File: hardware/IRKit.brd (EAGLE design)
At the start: 54 x 56 mm, 71 parts, among them CN1 USB-CONNECTORMICROB, IC1 ATMEGA32U4AU, IC2 TLV70233DBVT, IC3 LM386MM-1, IC4 GS1011MXXS, SW1 EVQPUJ02K, T1 2SD1781K, T2 BSS138

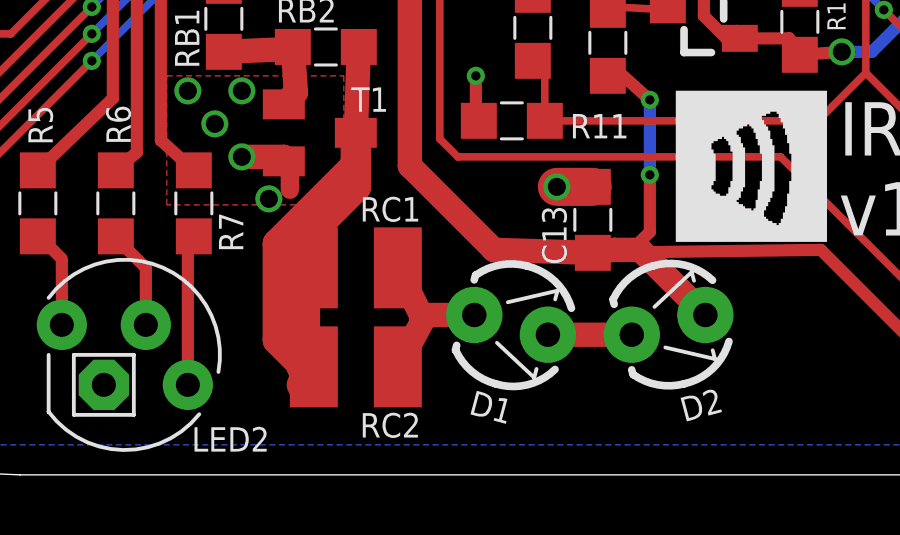
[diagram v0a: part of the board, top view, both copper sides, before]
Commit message: C13 1uF -> 4.7uF 1uF couldn't stop atmega32u4 from resetting when sending IR
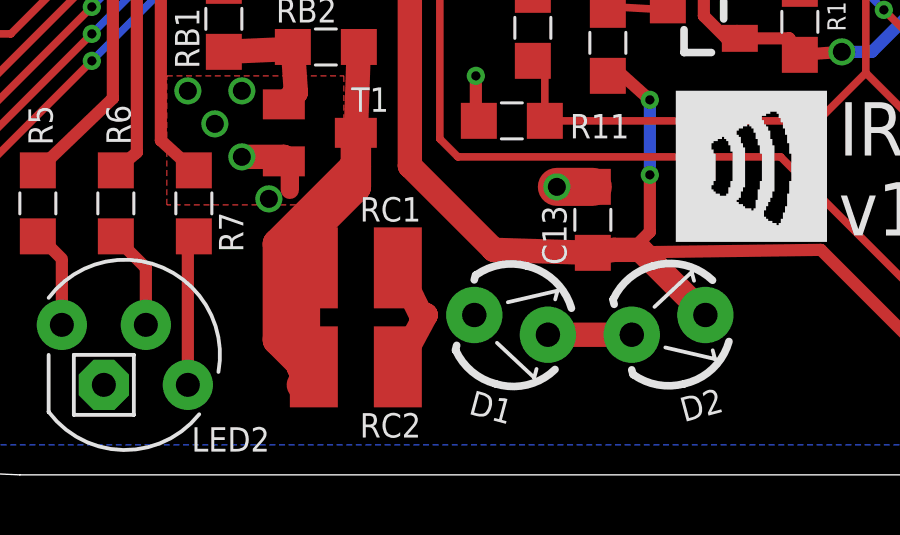
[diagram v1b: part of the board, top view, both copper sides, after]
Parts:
- C13: value 1uF -> 4.7uF
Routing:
- net IRLED: track 5.49 -> 3.87 mm
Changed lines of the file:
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@@
 <attribute name="VALUE" x="40.6" y="47.8" size="1.016" layer="27" rot="R180"/>
 </element>
-<element name="C13" library="my" package="SMD2012" value="1uF" x="27.1" y="8.5" smashed="yes" rot="R90">
+<element name="C13" library="my" package="SMD2012" value="4.7uF" x="27.1" y="8.5" smashed="yes" rot="R90">
 <attribute name="NAME" x="26.225" y="7" size="0.8128" layer="25" rot="R90"/>
 <attribute name="VALUE" x="29" y="7.5" size="1.016" layer="27" rot="R90"/>
@@
 </signal>
 <signal name="IRLED" class="2">
-<contactref element="D1" pad="K"/>
 <contactref element="RC2" pad="2"/>
 <contactref element="RC1" pad="2"/>
-<wire x1="23.148271875" y1="5.3287" x2="21.5287" y2="5.3287" width="0.8128" layer="1"/>
 <wire x1="21.5287" y1="5.3287" x2="20.6" y2="3.6" width="0.8128" layer="1"/>
 <wire x1="21.5287" y1="5.3287" x2="21.3713" y2="5.3287" width="0.8128" layer="1"/>
 <wire x1="21.3713" y1="5.3287" x2="20.6" y2="6.9" width="0.8128" layer="1"/>
+<contactref element="D1" pad="K"/>
+<wire x1="21.5287" y1="5.3287" x2="23.148271875" y2="5.3287" width="0" layer="19" extent="1-1"/>
 </signal>
 <signal name="+3V3" class="4">

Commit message: more specific value
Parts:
- T1: value 2SD1781K -> 2SD1781KT146Q
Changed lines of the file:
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@@
 <attribute name="VALUE" x="30.1005" y="49.639" size="0.8128" layer="27"/>
 </element>
-<element name="T1" library="transistor" package="SC59-BEC" value="2SD1781K" x="18" y="11.4" smashed="yes" rot="R270">
+<element name="T1" library="transistor" package="SC59-BEC" value="2SD1781KT146Q" x="18" y="11.4" smashed="yes" rot="R270">
 <attribute name="NAME" x="19.046" y="12.102" size="0.8128" layer="25"/>
 <attribute name="VALUE" x="14.698" y="13.94" size="0.8128" layer="27" ratio="10" rot="R270"/>

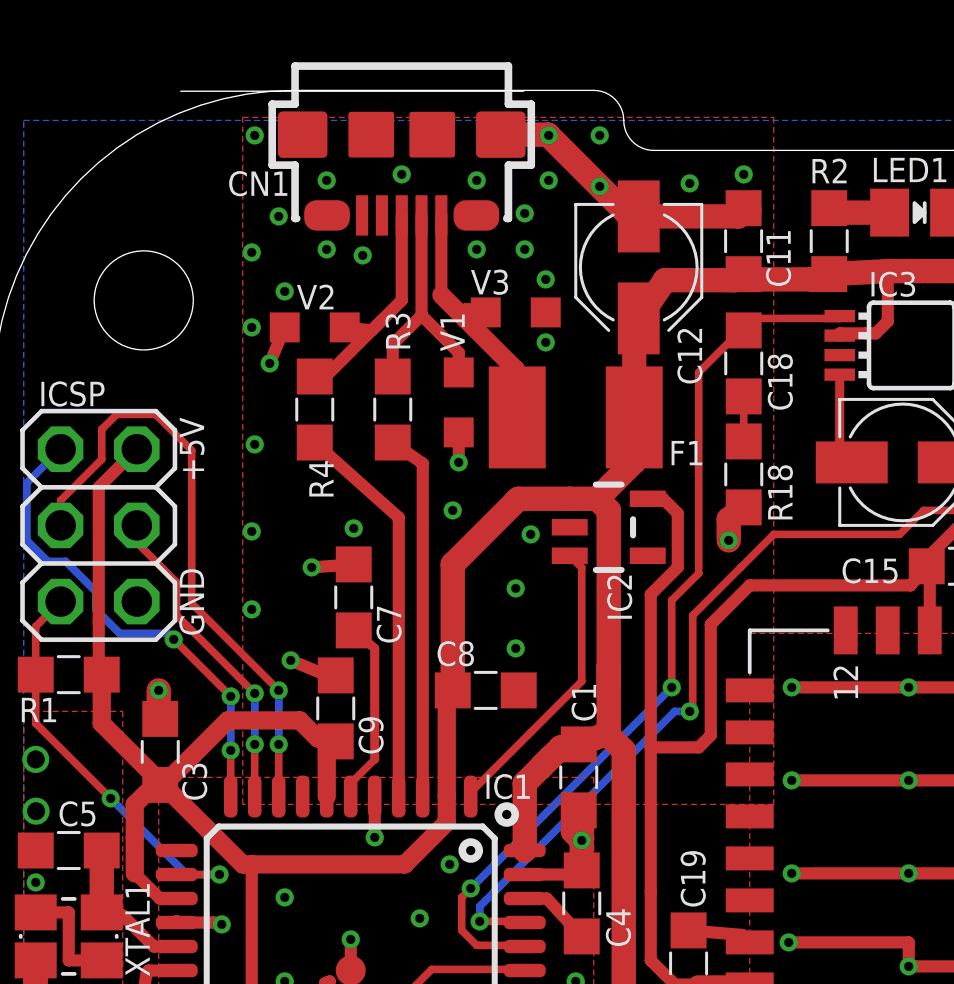
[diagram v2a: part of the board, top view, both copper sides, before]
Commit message: updated usb connector pattern with hirose's recommended pattern
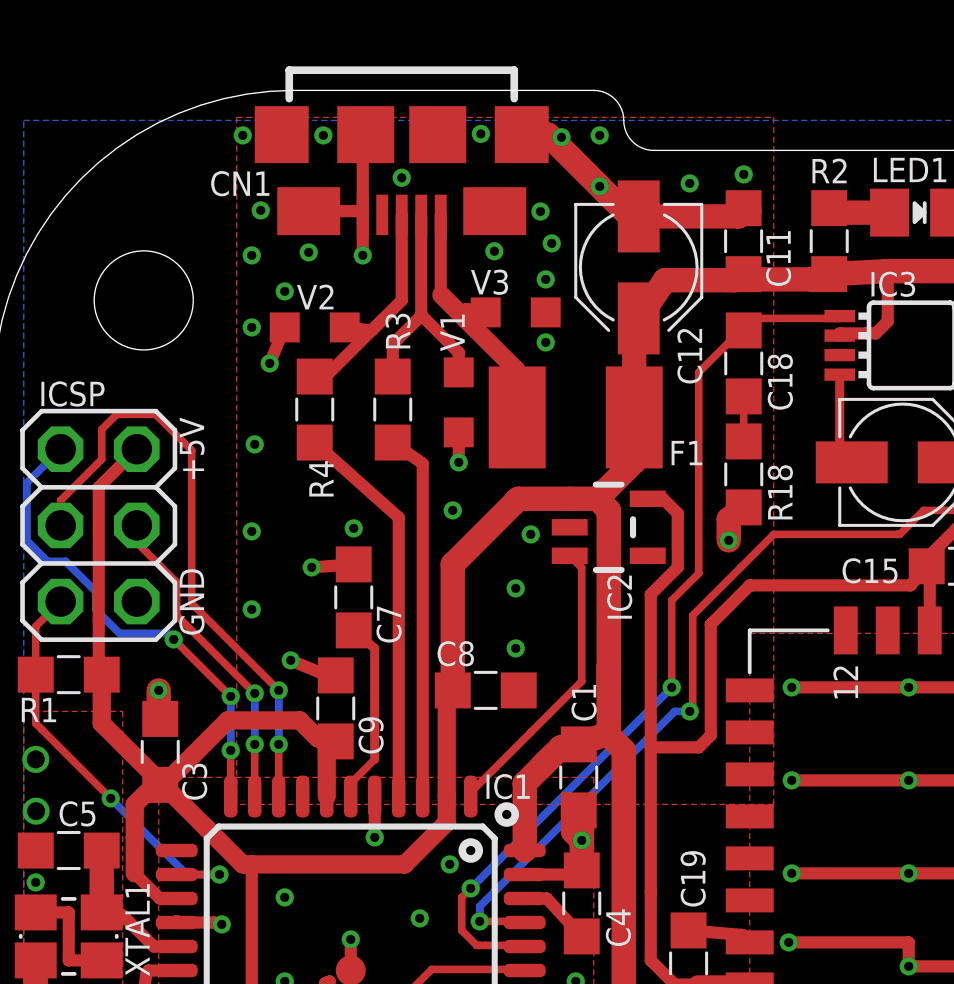
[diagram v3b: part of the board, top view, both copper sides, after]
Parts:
- CN1: value USB-CONNECTORMICROB -> ZX62-B-5PA(11)
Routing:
- net GND: track 190.6 -> 196.3 mm, vias 114 -> 113
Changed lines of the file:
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@@
 <attribute name="VALUE" x="21.786" y="32.338" size="0.8128" layer="27" rot="R90"/>
 </element>
-<element name="CN1" library="my" package="USB-MICROB" value="USB-CONNECTORMICROB" x="13.6" y="54.525" smashed="yes" rot="R180">
-<attribute name="NAME" x="7.79" y="52.485" size="0.8128" layer="21"/>
+<element name="CN1" library="my" package="USB-MICROB" value="ZX62-B-5PA(11)" x="13.6" y="54.525" smashed="yes" rot="R180">
+<attribute name="NAME" x="7.19" y="52.485" size="0.8128" layer="21"/>
 </element>
 <element name="C8" library="my" package="SMD2012" value="0.1uF" x="16.4" y="36" smashed="yes" rot="R180">
@@
 <contactref element="IC1" pad="5"/>
 <contactref element="CN1" pad="S1"/>
-<contactref element="CN1" pad="P5"/>
 <contactref element="IC2" pad="2"/>
 <contactref element="CN1" pad="S2"/>
@@
 <polygon width="0.4064" layer="1" isolate="0.254">
 <vertex x="26" y="32.2"/>
-<vertex x="8.3" y="32.2"/>
-<vertex x="8.3" y="55.1"/>
+<vertex x="8.1" y="32.2"/>
+<vertex x="8.1" y="55.1"/>
 <vertex x="26" y="55.1"/>
 </polygon>
 <via x="8.6" y="38.7" extent="1-16" drill="0.3048"/>
 <via x="12" y="41.4" extent="1-16" drill="0.3048"/>
-<via x="11.1" y="50.7" extent="1-16" drill="0.3048"/>
-<via x="8.7" y="54.5" extent="1-16" drill="0.3048"/>
+<via x="10.5" y="50.6" extent="1-16" drill="0.3048"/>
+<via x="8.3" y="54.5" extent="1-16" drill="0.3048"/>
 <via x="8.6" y="41.3" extent="1-16" drill="0.3048"/>
 <via x="8.7" y="44.2" extent="1-16" drill="0.3048"/>
@@
 <via x="17.4" y="37.4" extent="1-16" drill="0.3048"/>
 <via x="7.6" y="25.2" extent="1-16" drill="0.3048"/>
-<via x="16.1" y="50.7" extent="1-16" drill="0.3048"/>
+<via x="16.6875" y="50.6375" extent="1-16" drill="0.3048"/>
 <via x="18.4" y="47.6" extent="1-16" drill="0.3048"/>
-<via x="18.5" y="54.5" extent="1-16" drill="0.3048"/>
+<via x="18.925" y="54.4375" extent="1-16" drill="0.3048"/>
 <contactref element="V2" pad="2"/>
 <contactref element="V1" pad="2"/>
@@
 <vertex x="12.9" y="9"/>
 </polygon>
-<via x="13.6" y="53.2" extent="1-16" drill="0.3048"/>
-<via x="16.1" y="53" extent="1-16" drill="0.3048"/>
-<via x="17.7" y="51.9" extent="1-16" drill="0.3048"/>
-<via x="11.1" y="53" extent="1-16" drill="0.3048"/>
-<via x="9.5" y="51.8" extent="1-16" drill="0.3048"/>
+<via x="13.6" y="53.0875" extent="1-16" drill="0.3048"/>
+<via x="16.2375" y="54.55" extent="1-16" drill="0.3048"/>
+<via x="18.225" y="51.9625" extent="1-16" drill="0.3048"/>
+<via x="10.9875" y="54.5" extent="1-16" drill="0.3048"/>
+<via x="8.9" y="52" extent="1-16" drill="0.3048"/>
 <via x="19.4" y="26.3" extent="1-16" drill="0.3048"/>
 <via x="19.4" y="22.2" extent="1-16" drill="0.3048"/>
@@
 <wire x1="43.45" y1="55.05" x2="44.2" y2="54.3" width="0.6096" layer="1"/>
 <wire x1="21.3" y1="51.7" x2="18.475" y2="54.525" width="0.8128" layer="1"/>
-<wire x1="18.475" y1="54.525" x2="16.902" y2="54.525" width="0.8128" layer="1"/>
+<wire x1="18.475" y1="54.525" x2="17.6" y2="54.525" width="0.8128" layer="1"/>
 <wire x1="25.2" y1="52" x2="25.1" y2="52.1" width="0.8128" layer="1"/>
 <via x="20.2" y="54.5" extent="1-16" drill="0.3048"/>
@@
 <wire x1="43.8" y1="38" x2="43.8" y2="40" width="0.4064" layer="1"/>
 <wire x1="43.8" y1="40" x2="43.7" y2="40.4" width="0.4064" layer="1"/>
-<wire x1="12.8" y1="54.4" x2="12.584" y2="54.525" width="0.4064" layer="1"/>
+<wire x1="12.8" y1="54.4" x2="12.4" y2="54.525" width="0.4064" layer="1"/>
 <via x="34.1" y="47.1" extent="1-16" drill="0.3048"/>
 <wire x1="33" y1="47.175" x2="34.125" y2="47.175" width="0.4064" layer="1"/>
@@
 <wire x1="42.7" y1="51.7" x2="42.8" y2="51.6" width="0.4064" layer="1"/>
 <wire x1="42.8" y1="51.6" x2="42.8" y2="50.4" width="0.4064" layer="1"/>
-<wire x1="12.8" y1="54.4" x2="12.584" y2="54.525" width="0.4064" layer="1"/>
+<wire x1="12.8" y1="54.4" x2="12.4" y2="54.525" width="0.4064" layer="1"/>
 <wire x1="11.2" y1="26.3" x2="11.0413125" y2="26.23426875" width="0.4064" layer="1"/>
 <wire x1="11.2" y1="26.3" x2="11.0413125" y2="26.23426875" width="0.4064" layer="1"/>
@@
 <wire x1="21.5" y1="51.8" x2="24.8225" y2="51.8" width="0.8128" layer="1"/>
 <wire x1="24.8225" y1="51.8" x2="24.996" y2="52.0735" width="0.8128" layer="1"/>
-<via x="8.6" y="50.6" extent="1-16" drill="0.3048"/>
-<via x="18.5" y="53" extent="1-16" drill="0.3048"/>
-<via x="17.7" y="50.7" extent="1-16" drill="0.3048"/>
+<via x="8.6" y="50.5" extent="1-16" drill="0.3048"/>
+<via x="18.6" y="50.9" extent="1-16" drill="0.3048"/>
 <contactref element="T1" pad="E"/>
 <wire x1="16.8" y1="10.45" x2="17" y2="10.45" width="0.6096" layer="1"/>
@@
 <wire x1="2.5" y1="28.6" x2="2.5" y2="27" width="0.4064" layer="1"/>
 <wire x1="2.5" y1="27" x2="3.6" y2="27" width="0.4064" layer="1"/>
+<contactref element="CN1" pad="P5"/>
+<wire x1="12.3" y1="51.85" x2="12.3" y2="50.5" width="0.4064" layer="1"/>
+<wire x1="10.5" y1="51.975" x2="12.3" y2="51.975" width="0.4064" layer="1"/>
+<wire x1="12.3" y1="51.975" x2="12.3" y2="51.85" width="0.4064" layer="1"/>
+<wire x1="12.4" y1="54.525" x2="12.3" y2="54.525" width="0.4064" layer="1"/>
+<wire x1="12.3" y1="54.525" x2="12.3" y2="51.85" width="0.4064" layer="1"/>
 </signal>
 <signal name="N$10">
@@
 <contactref element="R3" pad="2"/>
 <contactref element="V1" pad="1"/>
-<wire x1="14.2604" y1="51.8326" x2="14.2604" y2="48.5" width="0.4064" layer="1"/>
 <wire x1="13.3" y1="46.4625" x2="13.3" y2="47.5396" width="0.4064" layer="1"/>
 <wire x1="13.3" y1="47.5396" x2="14.2604" y2="48.5" width="0.4064" layer="1"/>
 <wire x1="14.2604" y1="48.5" x2="15.5" y2="47.2604" width="0.4064" layer="1"/>
 <wire x1="15.5" y1="47.2604" x2="15.5" y2="46.6" width="0.4064" layer="1"/>
+<wire x1="14.2604" y1="48.5" x2="14.25" y2="48.5" width="0.4064" layer="1"/>
+<wire x1="14.25" y1="48.5" x2="14.25" y2="51.85" width="0.4064" layer="1"/>
 </signal>
 <signal name="N$51">
 <contactref element="CN1" pad="P3"/>
 <contactref element="R4" pad="2"/>
-<wire x1="13.6" y1="51.8326" x2="13.6" y2="49" width="0.4064" layer="1"/>
 <wire x1="13.6" y1="49" x2="12.95" y2="48.35" width="0.4064" layer="1"/>
 <wire x1="12.95" y1="48.35" x2="11.1625" y2="46.5625" width="0.4064" layer="1"/>
@@
 <wire x1="11.7" y1="48.1" x2="12.6" y2="48" width="0.4064" layer="1"/>
 <wire x1="12.6" y1="48" x2="12.95" y2="48.35" width="0.4064" layer="1"/>
+<wire x1="13.6" y1="49" x2="13.6" y2="51.85" width="0.4064" layer="1"/>
 </signal>
 <signal name="N$52">
 <contactref element="CN1" pad="P1"/>
 <contactref element="F1" pad="1"/>
-<wire x1="14.9208" y1="51.8326" x2="14.9208" y2="49.1792" width="0.4064" layer="1"/>
 <wire x1="16" y1="48.1" x2="17.4" y2="46.7" width="0.6096" layer="1"/>
 <wire x1="17.4" y1="46.7" x2="17.4" y2="45.5" width="0.6096" layer="1"/>
@@
 <wire x1="16.4" y1="48.6" x2="15.75" y2="48.6" width="0.6096" layer="1"/>
 <wire x1="15.75" y1="48.6" x2="15.75" y2="48.35" width="0.6096" layer="1"/>
+<wire x1="14.9208" y1="49.1792" x2="14.9" y2="49.1792" width="0.4064" layer="1"/>
+<wire x1="14.9" y1="49.1792" x2="14.9" y2="51.85" width="0.4064" layer="1"/>
 </signal>
 <signal name="D2">

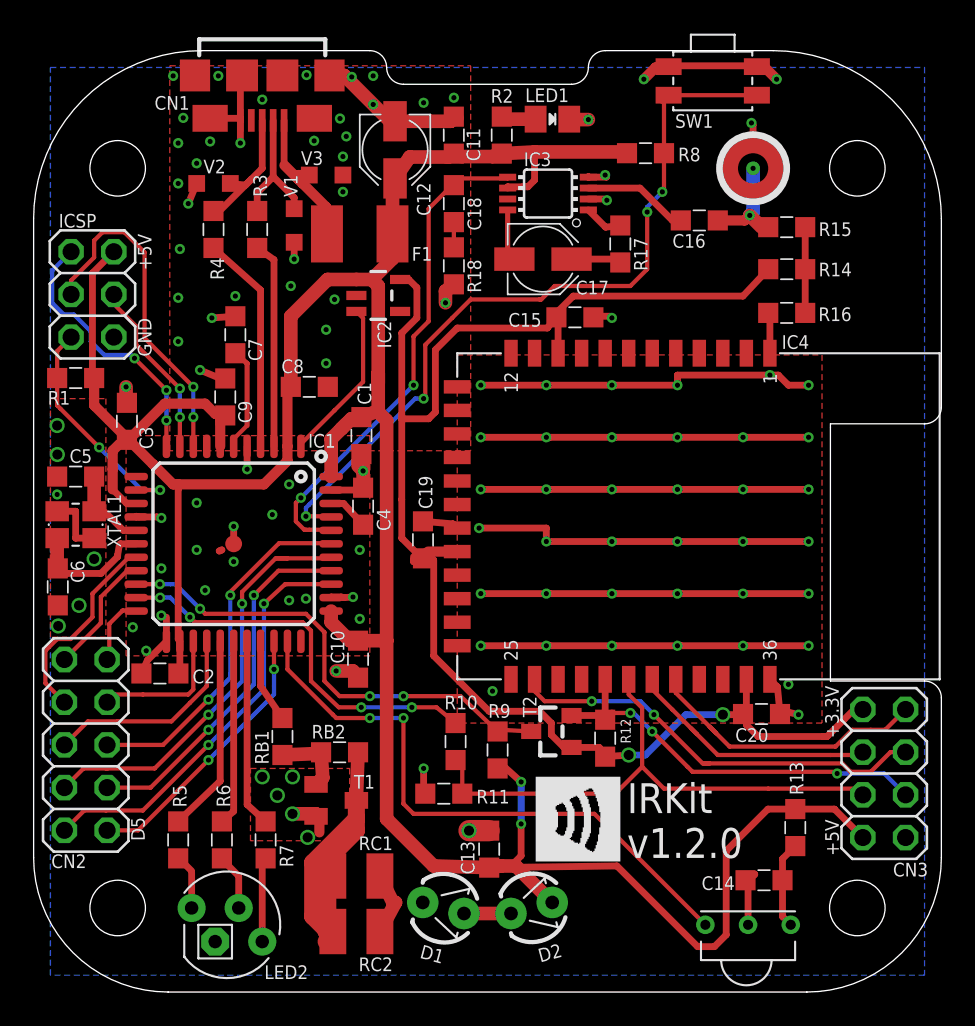
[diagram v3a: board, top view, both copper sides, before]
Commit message: fixed DRC errors around MIC fatter lines around IR LED
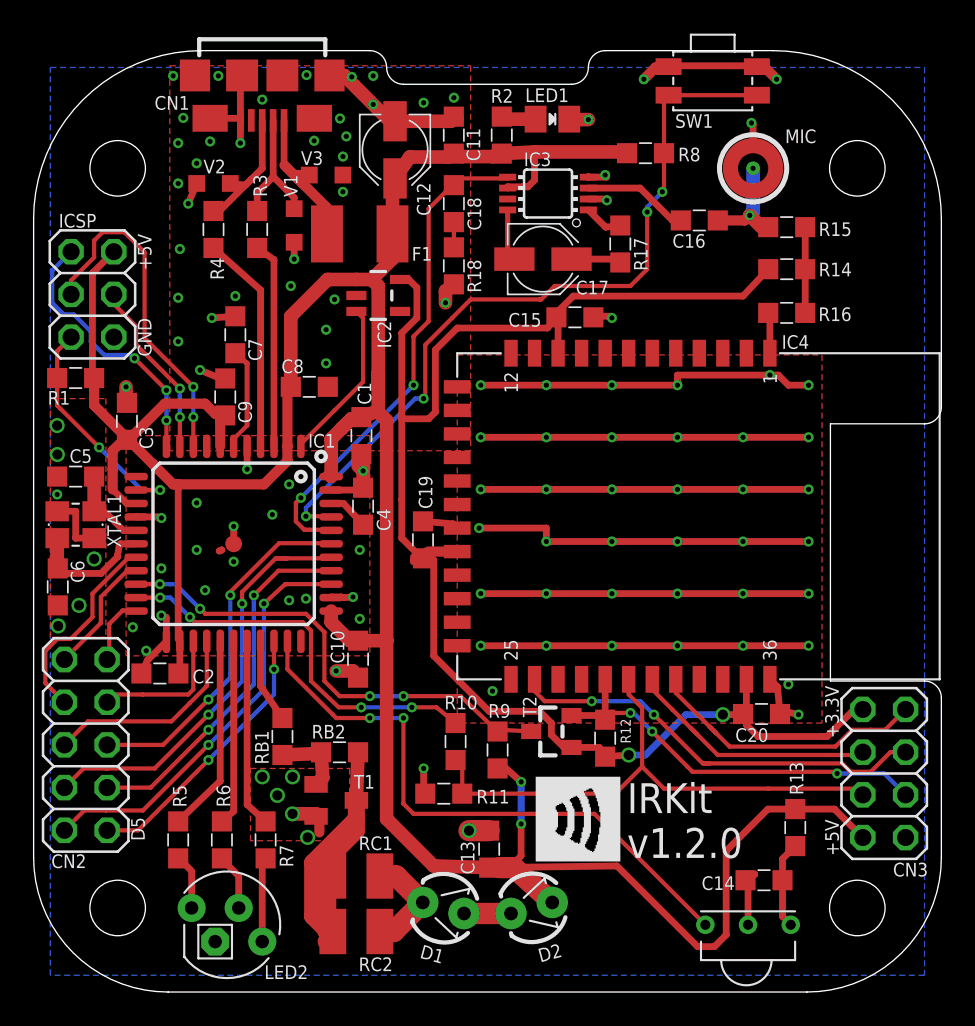
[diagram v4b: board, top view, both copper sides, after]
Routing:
- net IRLED: track 3.87 -> 6.46 mm
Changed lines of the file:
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@@
 <attribute name="VALUE" x="33.14" y="50.802" size="1.27" layer="27" ratio="10" rot="R180"/>
 </element>
-<element name="MIC" library="my" package="MIC_SMD_4MM" value="kus0223" x="42.8" y="49" smashed="yes"/>
+<element name="MIC" library="my" package="MIC_SMD_4MM" value="kus0223" x="42.8" y="49" smashed="yes">
+<attribute name="NAME" x="44.7" y="50.5" size="0.8128" layer="25"/>
+<attribute name="VALUE" x="44.7" y="46.8" size="0.8128" layer="27"/>
+</element>
 <element name="R15" library="my" package="SMD2012" value="2k" x="44.8" y="45.5" smashed="yes">
 <attribute name="NAME" x="46.7" y="44.975" size="0.8128" layer="25"/>
@@
 <contactref element="D2" pad="A"/>
 <wire x1="23.8" y1="7.5" x2="27.1" y2="7.4" width="0.8128" layer="1"/>
-<wire x1="27.1" y1="7.4" x2="27.8" y2="7.5" width="0.8128" layer="1"/>
-<wire x1="27.8" y1="7.5" x2="28.680425" y2="7.5" width="0.8128" layer="1"/>
-<wire x1="28.680425" y1="7.5" x2="30.851725" y2="5.3287" width="0.8128" layer="1"/>
+<wire x1="27.1" y1="7.4" x2="27.7" y2="7.4" width="0.8128" layer="1"/>
+<wire x1="27.7" y1="7.4" x2="28.580425" y2="7.4" width="1.27" layer="1"/>
+<wire x1="28.580425" y1="7.4" x2="30.851725" y2="5.3287" width="1.27" layer="1"/>
 <wire x1="29" y1="8.1" x2="28.4" y2="7.5" width="0.4064" layer="1"/>
-<wire x1="28.4" y1="7.5" x2="27.8" y2="7.5" width="0.4064" layer="1"/>
+<wire x1="28.4" y1="7.5" x2="27.7" y2="7.4" width="0.4064" layer="1"/>
 <wire x1="34.7" y1="7.5" x2="27.1" y2="7.4" width="0.4064" layer="1"/>
 <wire x1="41.2" y1="3.4" x2="41.2" y2="8.4" width="0.4064" layer="1"/>
@@
 <contactref element="RC2" pad="2"/>
 <contactref element="RC1" pad="2"/>
-<wire x1="21.5287" y1="5.3287" x2="20.6" y2="3.6" width="0.8128" layer="1"/>
-<wire x1="21.5287" y1="5.3287" x2="21.3713" y2="5.3287" width="0.8128" layer="1"/>
-<wire x1="21.3713" y1="5.3287" x2="20.6" y2="6.9" width="0.8128" layer="1"/>
 <contactref element="D1" pad="K"/>
-<wire x1="21.5287" y1="5.3287" x2="23.148271875" y2="5.3287" width="0" layer="19" extent="1-1"/>
+<wire x1="23.148271875" y1="5.3287" x2="21.576971875" y2="6.9" width="1.27" layer="1"/>
+<wire x1="21.576971875" y1="6.9" x2="20.6" y2="6.9" width="1.27" layer="1"/>
+<wire x1="23.148271875" y1="5.3287" x2="21.419571875" y2="3.6" width="1.27" layer="1"/>
+<wire x1="21.419571875" y1="3.6" x2="20.6" y2="3.6" width="1.27" layer="1"/>
 </signal>
 <signal name="+3V3" class="4">
@@
 <contactref element="D1" pad="A"/>
 <contactref element="D2" pad="K"/>
-<wire x1="25.601725" y1="4.671296875" x2="28.398271875" y2="4.671296875" width="0.8128" layer="1"/>
+<wire x1="25.601725" y1="4.671296875" x2="28.398271875" y2="4.671296875" width="1.27" layer="1"/>
 </signal>
 <signal name="UCAP">
